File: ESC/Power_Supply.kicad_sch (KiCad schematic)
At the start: 12 parts, among them IC6 BD433M5FP-CE2

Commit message: Power Supply Update
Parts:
- removed L1: 10uH 2.2A 20%, BassingaLib_Inductors:BWVS00505040100M00, symbol BassingaLib_Inductors:BWVS00505040100M00
- added C40, C43: GXC1V221MCQ1GS, BassingaLib_Capacitors:CAPAE1030X1080N, symbol BassingaLib_Capacitors:GXC1V221MCQ1GS
- added C44: 10uF 63V, Capacitor_SMD:C_1210_3225Metric, symbol Device:C
- added J5: XT30PW-M, BassinaLib_Connectors:AMASS_XT30PW-M, symbol BassinaLib_Connectors:XT30PW-M
- added L2: 10uH 2.2A 20%, BassingaLib_Inductors:BWVS00505040100M00, symbol BassingaLib_Inductors:BWVS00505040100M00
- added R50: 0R 1%, Resistor_SMD:R_0603_1608Metric, symbol Device:R
- renumbered C40 to C38, C42 to C39, C36 to C41, C41 to C42, C37 to C45, C38 to C46, C39 to C47
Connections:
- net +12V: now also L2.2
- net GND: now also R50.1
- net at C41.1, PS1.5 (SW): now also L2.1
- new net: C40.1 (+), C43.1 (+), C44.2, J5.P
- new net Power_GND: C40.2 (-), C43.2 (-), C44.1, J5.N, R50.2
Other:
- moved on the sheet: C38, C39, C41, C42, C45, C46, C47, IC6, PS1, R48, R49

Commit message: Update 20.07.2025
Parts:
- added D11: SS0540_R1_00001, BassingaLib_Diodes:SOD3816X135N, symbol BassingaLib_Diodes:SS0540_R1_00001
- added LED2: RED LED, BassinaLib_LEDs:LEDM168X80N, symbol BassinaLib_LEDs:APHD1608LSURCK
- added LED3, LED4: GREEN, BassinaLib_LEDs:LEDM168X80N, symbol BassinaLib_LEDs:APHD1608LZGCK
- added R50: 18k 1%, Resistor_SMD:R_0603_1608Metric, symbol Device:R
- added R52: 10k 1%, Resistor_SMD:R_0603_1608Metric, symbol Device:R
- added R53: 680R 1%, Resistor_SMD:R_0603_1608Metric, symbol Device:R
- R49: Manufacturer_Part_Number AC0603FR-0718KL -> AC0603FR-1318KL
- renumbered C38 to C39, C39 to C40, C40 to C41, C41 to C42, C42 to C43, C43 to C44, C44 to C45, C45 to C46, C46 to C47, C47 to C48, L2 to L1, R50 to R51
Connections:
- net +12V: now also R52.1
- net +3.3V: now also R53.1
- net GND: now also LED3.1 (K), LED4.1 (K)
- net Power_GND: now also D11.2 (A), LED2.1 (K)
- net at C41.1 (+), C44.1 (+), C45.2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: now also D11.1 (K)
- new net: LED3.2 (A), R52.2
- new net: LED4.2 (A), R53.2
- new net: LED2.2 (A), R50.1
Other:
- moved on the sheet: C39, C40, C41, C42, C43, C44, C45, C46, C47, C48, IC6, J5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

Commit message: End of Schematic
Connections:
- net at R50.1: no longer LED2.2 (A)
- net at R50.2: now also LED2.2 (A)
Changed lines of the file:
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@@
 	(wire
 		(pts
+			(xy 223.52 95.25) (xy 223.52 101.6)
+		)
+		(stroke
+			(width 0)
+			(type default)
+		)
+	)
+	(wire
+		(pts
 			(xy 153.67 109.22) (xy 137.16 109.22)
 		)
@@
 	(wire
 		(pts
-			(xy 223.52 95.25) (xy 223.52 101.6)
-		)
-		(stroke
-			(width 0)
-			(type default)
-		)
-	)
-	(wire
-		(pts
 			(xy 46.99 99.06) (xy 52.07 99.06)
 		)
@@
 			)
 		)
-		(property "Value" "6S_Power"
+		(property "Value" "+22V"
 			(at 34.29 85.09 0)
 			(effects
@@
 		(lib_id "Device:R")
 		(at 223.52 91.44 0)
-		(mirror x)
+		(mirror y)
 		(unit 1)
 		(exclude_from_sim no)
@@
 		(dnp no)
 		(property "Reference" "R50"
-			(at 220.472 89.662 90)
+			(at 226.568 93.218 90)
 			(effects
 				(font
@@
 		)
 		(property "Value" "18k 1%"
-			(at 226.822 88.138 90)
+			(at 220.218 94.742 90)
 			(effects
 				(font
@@
 		)
 		(property "Footprint" "Resistor_SMD:R_0603_1608Metric"
-			(at 221.742 91.44 90)
+			(at 225.298 91.44 90)
 			(effects
 				(font
@@
 		(dnp no)
 		(fields_autoplaced yes)
-		(property "Reference" "#PWR0100"
+		(property "Reference" "#PWR093"
 			(at 223.52 127.508 0)
 			(effects
@@
 			(project "ESC"
 				(path "/7036a814-0f41-4c6c-a077-a78d90a22423/50e6b873-fcc8-4519-931d-a1e0dcbcbe76"
-					(reference "#PWR0100")
+					(reference "#PWR093")
 					(unit 1)
 				)
@@
 			)
 		)
-		(property "Value" "6S_Power"
+		(property "Value" "+22V"
 			(at 127 21.59 0)
 			(effects
@@
 			)
 		)
-		(property "Value" "6S_Power"
+		(property "Value" "+22V"
 			(at 223.52 76.2 0)
 			(effects

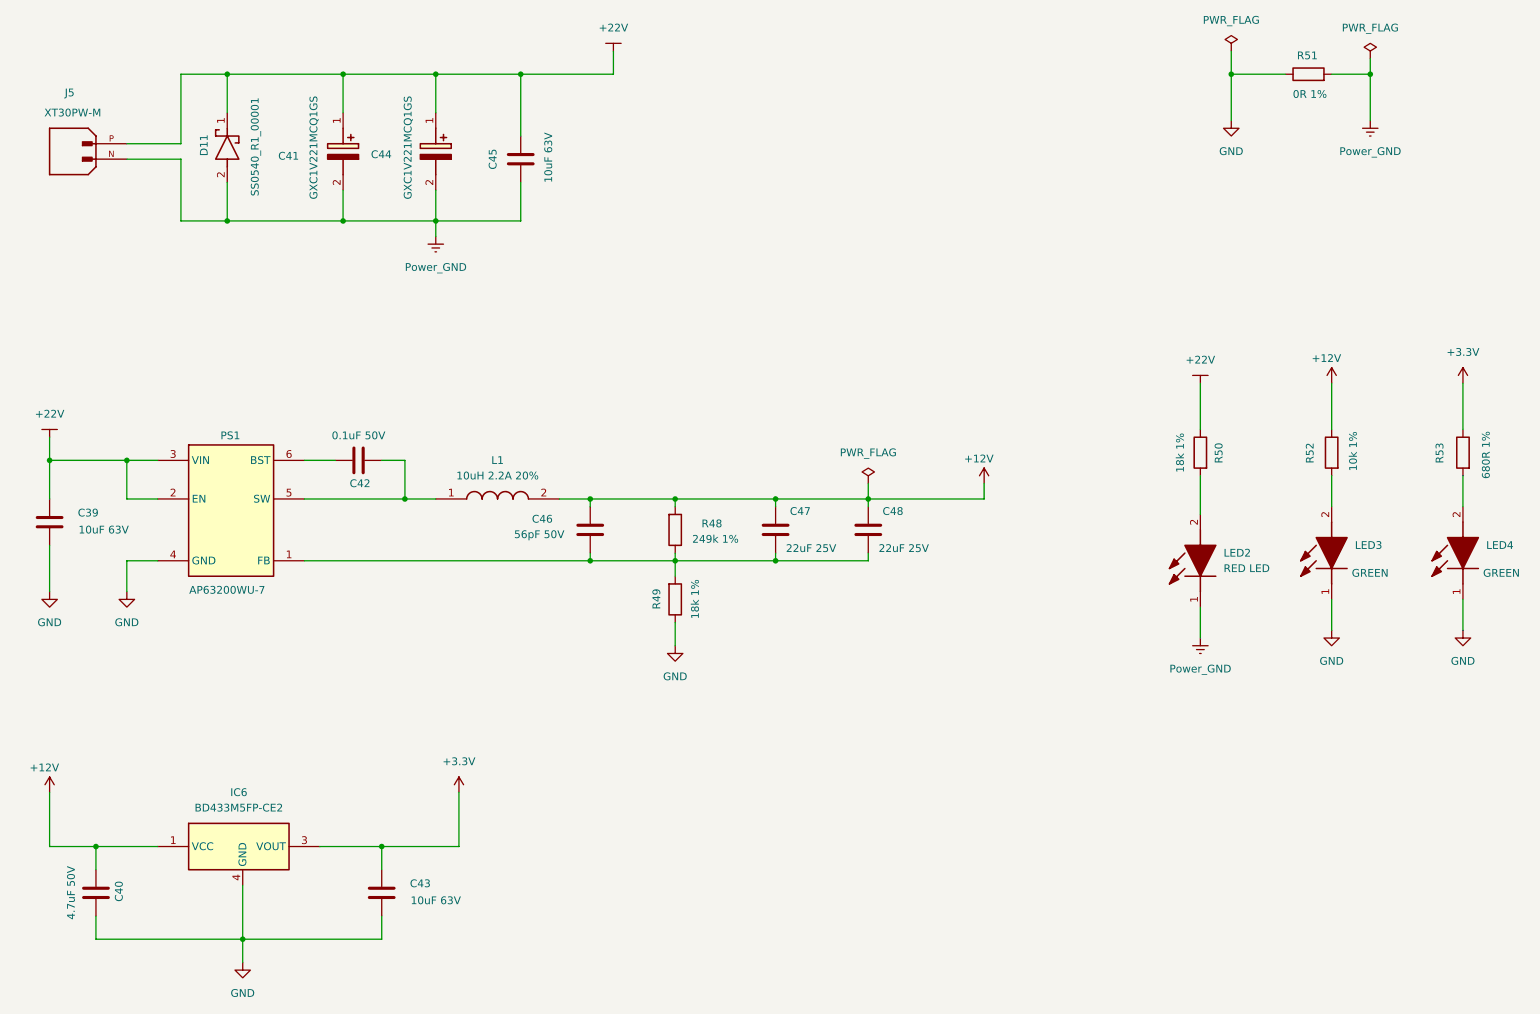
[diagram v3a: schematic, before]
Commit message: Start of PCB Layout
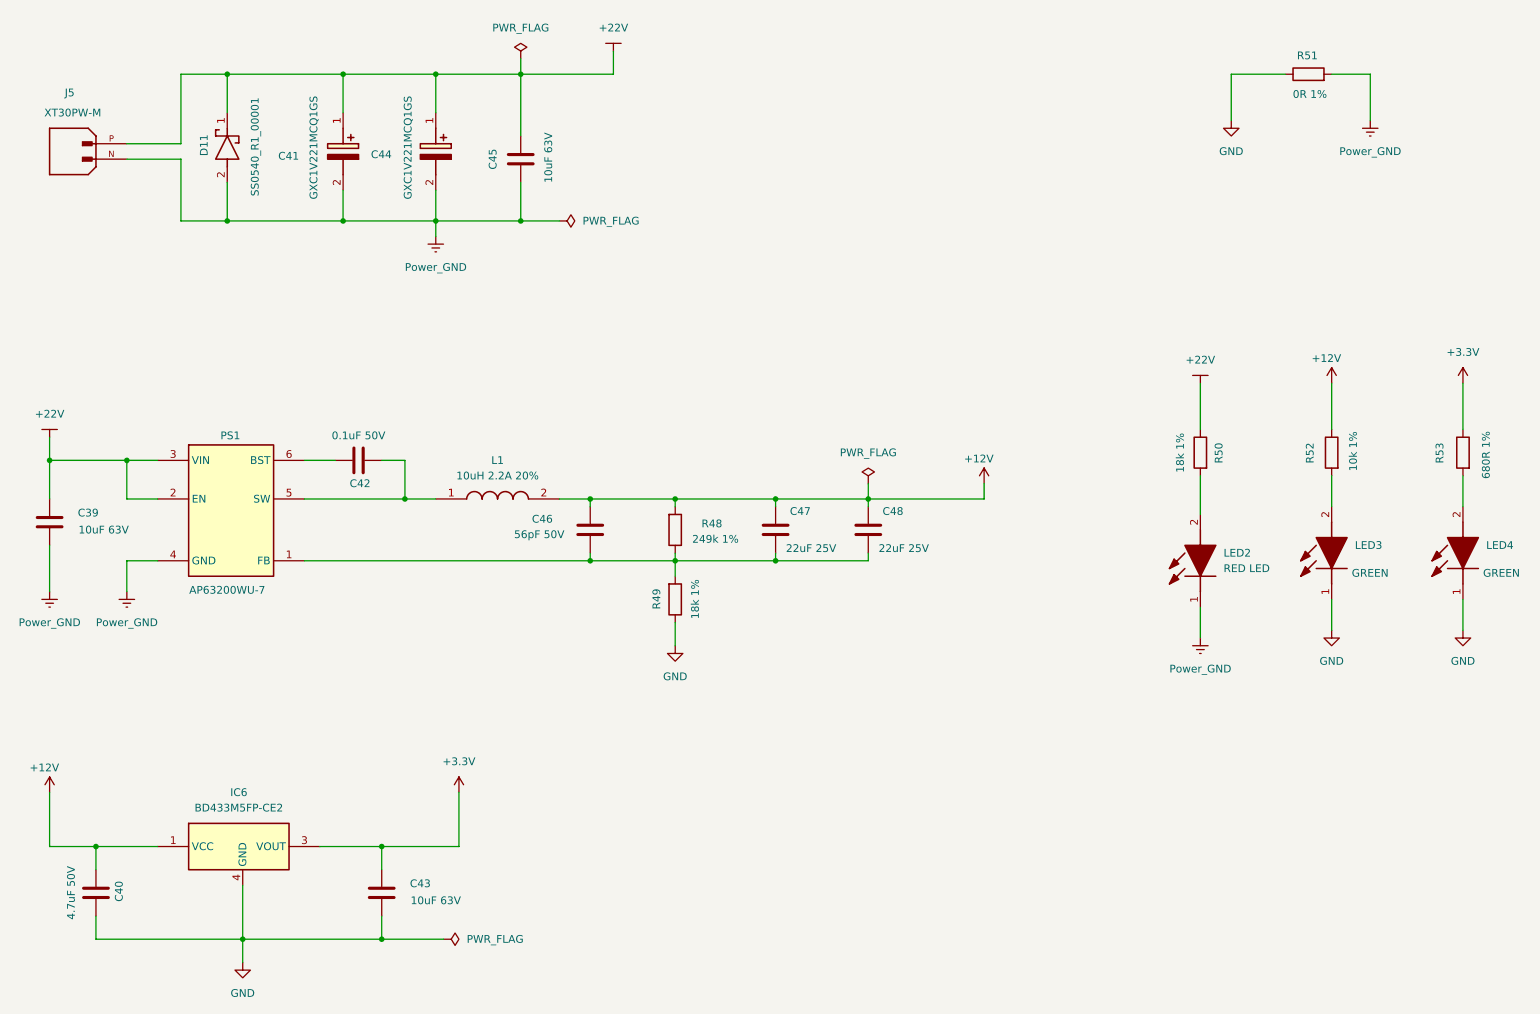
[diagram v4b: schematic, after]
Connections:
- net GND: no longer C39.1, PS1.4 (GND)
- net Power_GND: now also C39.1, PS1.4 (GND)
- net +22V: now reaches C41.1 (+), C44.1 (+), C45.2, D11.1 (K), J5.P
- net +22V: now also C39.2, PS1.2 (EN), PS1.3 (VIN), R50.1

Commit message: PCB Layout Update
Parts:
- removed R51: 0R 1%, Resistor_SMD:R_0603_1608Metric, symbol Device:R
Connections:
- net Power_GND is gone; now on net GND: C39.1, C41.2 (-), C44.2 (-), C45.1, D11.2 (A), J5.N, LED2.1 (K), PS1.4 (GND)
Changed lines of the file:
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@@
 	(wire
 		(pts
-			(xy 237.49 29.21) (xy 228.6 29.21)
+			(xy 228.6 29.21) (xy 251.46 29.21)
 		)
 		(stroke
@@
 	(wire
 		(pts
-			(xy 245.11 29.21) (xy 251.46 29.21)
-		)
-		(stroke
-			(width 0)
-			(type default)
-		)
-	)
-	(wire
-		(pts
 			(xy 78.74 156.21) (xy 88.9 156.21)
 		)
@@
 					(unit 1)
 				)
-			)
-		)
-	)
-	(symbol
-		(lib_id "Device:R")
-		(at 241.3 29.21 90)
-		(unit 1)
-		(exclude_from_sim no)
-		(in_bom yes)
-		(on_board yes)
-		(dnp no)
-		(property "Reference" "R51"
-			(at 242.824 26.162 90)
-			(effects
-				(font
-					(size 1.27 1.27)
-				)
-				(justify left)
-			)
-		)
-		(property "Value" "0R 1%"
-			(at 244.348 32.512 90)
-			(effects
-				(font
-					(size 1.27 1.27)
-				)
-				(justify left)
-			)
-		)
-		(property "Footprint" "Resistor_SMD:R_0603_1608Metric"
-			(at 241.3 30.988 90)
-			(effects
-				(font
-					(size 1.27 1.27)
-				)
-				(hide yes)
-			)
-		)
-		(property "Datasheet" "https://www.mouser.fr/datasheet/2/447/Yageo_06282023_ACseries-3224032.pdf"
-			(at 241.3 29.21 0)
-			(effects
-				(font
-					(size 1.27 1.27)
-				)
-				(hide yes)
-			)
-		)
-		(property "Description" "Thick Film Resistors - SMD 0 Ohms 100mW 0603 1% AEC-Q200 Standard Power Version"
-			(at 241.3 29.21 0)
-			(effects
-				(font
-					(size 1.27 1.27)
-				)
-				(hide yes)
-			)
-		)
-		(property "Manufacturer_Name" "YAGEO"
-			(at 241.3 29.21 0)
-			(effects
-				(font
-					(size 1.27 1.27)
-				)
-				(hide yes)
-			)
-		)
-		(property "Manufacturer_Part_Number" "AC0603FR-070RL"
-			(at 241.3 29.21 0)
-			(effects
-				(font
-					(size 1.27 1.27)
-				)
-				(hide yes)
-			)
-		)
-		(property "Packaging" "0603 (608mm)"
-			(at 241.3 29.21 0)
-			(effects
-				(font
-					(size 1.27 1.27)
-				)
-				(hide yes)
-			)
-		)
-		(pin "1"
-		)
-		(pin "2"
-		)
-		(instances
-			(project "ESC"
-				(path "/7036a814-0f41-4c6c-a077-a78d90a22423/50e6b873-fcc8-4519-931d-a1e0dcbcbe76"
-					(reference "R51")
-					(unit 1)
-				)

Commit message: Update 25.07.2025
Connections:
- net GND: now also C47.1, C48.1
- net at C46.1, PS1.1 (FB), R48.1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: no longer C47.1, C48.1
- net SW: now reaches C42.1, L1.1, PS1.5 (SW)
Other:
- moved on the sheet: C47, C48, R49
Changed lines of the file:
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@@
 	)
 	(junction
+		(at 137.16 120.65)
+		(diameter 0)
+		(color 0 0 0 0)
+	)
+	(junction
+		(at 123.19 109.22)
+		(diameter 0)
+		(color 0 0 0 0)
+	)
+	(junction
 		(at 137.16 99.06)
 		(diameter 0)
@@
 	)
 	(junction
-		(at 111.76 29.21)
+		(at 153.67 120.65)
 		(diameter 0)
 		(color 0 0 0 0)
 	)
 	(junction
-		(at 97.79 29.21)
+		(at 111.76 29.21)
 		(diameter 0)
 		(color 0 0 0 0)
 	)
 	(junction
-		(at 34.29 92.71)
+		(at 97.79 29.21)
 		(diameter 0)
 		(color 0 0 0 0)
 	)
 	(junction
-		(at 153.67 109.22)
+		(at 34.29 92.71)
 		(diameter 0)
 		(color 0 0 0 0)
@@
 	)
 	(junction
-		(at 88.9 171.45)
-		(diameter 0)
-		(color 0 0 0 0)
-	)
-	(junction
-		(at 41.91 156.21)
+		(at 137.16 109.22)
 		(diameter 0)
 		(color 0 0 0 0)
 	)
 	(junction
-		(at 111.76 53.34)
+		(at 88.9 171.45)
 		(diameter 0)
 		(color 0 0 0 0)
 	)
 	(junction
-		(at 46.99 92.71)
+		(at 41.91 156.21)
 		(diameter 0)
 		(color 0 0 0 0)
 	)
 	(junction
-		(at 137.16 109.22)
+		(at 111.76 53.34)
 		(diameter 0)
 		(color 0 0 0 0)
 	)
 	(junction
-		(at 123.19 109.22)
+		(at 46.99 92.71)
 		(diameter 0)
 		(color 0 0 0 0)
@@
 	(wire
 		(pts
-			(xy 82.55 53.34) (xy 97.79 53.34)
+			(xy 123.19 107.95) (xy 123.19 109.22)
 		)
 		(stroke
@@
 	(wire
 		(pts
-			(xy 92.71 99.06) (xy 97.79 99.06)
+			(xy 82.55 53.34) (xy 97.79 53.34)
 		)
 		(stroke
@@
 	(wire
 		(pts
-			(xy 228.6 29.21) (xy 251.46 29.21)
+			(xy 92.71 99.06) (xy 97.79 99.06)
 		)
 		(stroke
@@
 	(wire
 		(pts
-			(xy 46.99 92.71) (xy 46.99 99.06)
+			(xy 228.6 29.21) (xy 251.46 29.21)
 		)
 		(stroke
@@
 	(wire
 		(pts
-			(xy 251.46 29.21) (xy 251.46 36.83)
+			(xy 46.99 92.71) (xy 46.99 99.06)
 		)
 		(stroke
@@
 	(wire
 		(pts
-			(xy 46.99 43.18) (xy 55.88 43.18)
+			(xy 251.46 29.21) (xy 251.46 36.83)
 		)
 		(stroke
@@
 	(wire
 		(pts
-			(xy 123.19 109.22) (xy 137.16 109.22)
+			(xy 46.99 43.18) (xy 55.88 43.18)
 		)
 		(stroke
@@
 	(wire
 		(pts
-			(xy 137.16 123.19) (xy 137.16 119.38)
+			(xy 137.16 123.19) (xy 137.16 120.65)
 		)
 		(stroke
@@
 	(wire
 		(pts
-			(xy 153.67 107.95) (xy 153.67 109.22)
+			(xy 76.2 109.22) (xy 123.19 109.22)
 		)
 		(stroke
@@
 	(wire
 		(pts
-			(xy 168.91 100.33) (xy 168.91 99.06)
+			(xy 168.91 105.41) (xy 168.91 99.06)
 		)
 		(stroke
@@
 	(wire
 		(pts
-			(xy 137.16 109.22) (xy 137.16 107.95)
+			(xy 137.16 107.95) (xy 137.16 109.22)
 		)
 		(stroke
@@
 	(wire
 		(pts
-			(xy 153.67 109.22) (xy 168.91 109.22)
+			(xy 153.67 120.65) (xy 168.91 120.65)
 		)
 		(stroke
@@
 	(wire
 		(pts
-			(xy 153.67 100.33) (xy 153.67 99.06)
+			(xy 153.67 105.41) (xy 153.67 99.06)
+		)
+		(stroke
+			(width 0)
+			(type default)
+		)
+	)
+	(wire
+		(pts
+			(xy 137.16 109.22) (xy 137.16 110.49)
 		)
 		(stroke
@@
 	(wire
 		(pts
-			(xy 153.67 109.22) (xy 137.16 109.22)
+			(xy 123.19 109.22) (xy 137.16 109.22)
 		)
 		(stroke
@@
 	(wire
 		(pts
-			(xy 76.2 109.22) (xy 123.19 109.22)
+			(xy 153.67 113.03) (xy 153.67 120.65)
 		)
 		(stroke
@@
 	(wire
 		(pts
+			(xy 137.16 118.11) (xy 137.16 120.65)
+		)
+		(stroke
+			(width 0)
+			(type default)
+		)
+	)
+	(wire
+		(pts
 			(xy 46.99 99.06) (xy 52.07 99.06)
 		)
@@
 	(wire
 		(pts
-			(xy 123.19 109.22) (xy 123.19 107.95)
+			(xy 137.16 120.65) (xy 153.67 120.65)
 		)
 		(stroke
@@
 	(wire
 		(pts
-			(xy 137.16 111.76) (xy 137.16 109.22)
-		)
-		(stroke
-			(width 0)
-			(type default)
-		)
-	)
-	(wire
-		(pts
 			(xy 41.91 156.21) (xy 52.07 156.21)
 		)
@@
 	(wire
 		(pts
-			(xy 168.91 107.95) (xy 168.91 109.22)
+			(xy 168.91 113.03) (xy 168.91 120.65)
 		)
 		(stroke
@@
 		)
 	)
+	(label "SW"
+		(at 78.74 99.06 0)
+		(effects
+			(font
+				(size 1.27 1.27)
+			)
+			(justify left bottom)
+		)
+	)
 	(symbol
 		(lib_id "power:GND")
@@
 	(symbol
 		(lib_id "Device:R")
-		(at 137.16 115.57 0)
+		(at 137.16 114.3 0)
 		(mirror x)
 		(unit 1)
@@
 		(dnp no)
 		(property "Reference" "R49"
-			(at 134.112 113.792 90)
+			(at 134.112 112.522 90)
 			(effects
 				(font
@@
 		)
 		(property "Value" "18k 1%"
-			(at 140.462 112.268 90)
+			(at 140.462 110.998 90)
 			(effects
 				(font
@@
 		)
 		(property "Footprint" "Resistor_SMD:R_0603_1608Metric"
-			(at 135.382 115.57 90)
+			(at 135.382 114.3 90)
 			(effects
 				(font
@@
 		)
 		(property "Datasheet" "https://www.mouser.fr/datasheet/2/447/PYu_AC_51_RoHS_L_11-3418659.pdf"
-			(at 137.16 115.57 0)
+			(at 137.16 114.3 0)
 			(effects
 				(font
@@
 		)
 		(property "Description" "Thick Film Resistors - SMD 18 kOhms 100mW 0603 1% AEC-Q200"
-			(at 137.16 115.57 0)
+			(at 137.16 114.3 0)
 			(effects
 				(font
@@
 		)
 		(property "Manufacturer_Name" "YAGEO"
-			(at 137.16 115.57 0)
+			(at 137.16 114.3 0)
 			(effects
 				(font
@@
 		)
 		(property "Manufacturer_Part_Number" "AC0603FR-1318KL"
-			(at 137.16 115.57 0)
+			(at 137.16 114.3 0)
 			(effects
 				(font
@@
 		)
 		(property "Packaging" "0603 (608mm)"
-			(at 137.16 115.57 0)
+			(at 137.16 114.3 0)
 			(effects
 				(font
@@
 	(symbol
 		(lib_id "Device:C")
-		(at 168.91 104.14 180)
+		(at 168.91 109.22 180)
 		(unit 1)
 		(exclude_from_sim no)
@@
 		(dnp no)
 		(property "Reference" "C48"
-			(at 172.974 101.092 0)
+			(at 172.974 106.172 0)
 			(effects
 				(font
@@
 		)
 		(property "Value" "22uF 25V"
-			(at 174.752 107.188 0)
+			(at 174.752 112.268 0)
 			(effects
 				(font
@@
 		)
 		(property "Footprint" "Capacitor_SMD:C_1210_3225Metric"
-			(at 167.9448 100.33 0)
+			(at 167.9448 105.41 0)
 			(effects
 				(font
@@
 		)
 		(property "Datasheet" "https://www.mouser.fr/datasheet/2/585/MLCC-1837944.pdf"
-			(at 168.91 104.14 0)
+			(at 168.91 109.22 0)
 			(effects
 				(font
@@
 		)
 		(property "Description" "Multilayer Ceramic Capacitors MLCC - SMD/SMT 22uF+/-10% 25V X7R 3 1210"
-			(at 168.91 104.14 0)
+			(at 168.91 109.22 0)
 			(effects
 				(font
@@
 		)
 		(property "Manufacturer_Name" "Samsung Electro-Mechanics"
-			(at 168.91 104.14 0)
+			(at 168.91 109.22 0)
 			(effects
 				(font
@@
 		)
 		(property "Manufacturer_Part_Number" "CL32B226KAJNNNE"
-			(at 168.91 104.14 0)
+			(at 168.91 109.22 0)
 			(effects
 				(font
@@
 		)
 		(property "Packaging" "1210 (3225mm)"
-			(at 168.91 104.14 0)
+			(at 168.91 109.22 0)
 			(effects
 				(font
@@
 	(symbol
 		(lib_id "Device:C")
-		(at 153.67 104.14 180)
+		(at 153.67 109.22 180)
 		(unit 1)
 		(exclude_from_sim no)
@@
 		(dnp no)
 		(property "Reference" "C47"
-			(at 157.734 101.092 0)
+			(at 157.734 106.172 0)
 			(effects
 				(font
@@
 		)
 		(property "Value" "22uF 25V"
-			(at 159.512 107.188 0)
+			(at 159.512 112.268 0)
 			(effects
 				(font
@@
 		)
 		(property "Footprint" "Capacitor_SMD:C_1210_3225Metric"
-			(at 152.7048 100.33 0)
+			(at 152.7048 105.41 0)
 			(effects
 				(font
@@
 		)
 		(property "Datasheet" "https://www.mouser.fr/datasheet/2/585/MLCC-1837944.pdf"
-			(at 153.67 104.14 0)
+			(at 153.67 109.22 0)
 			(effects
 				(font
@@
 		)
 		(property "Description" "Multilayer Ceramic Capacitors MLCC - SMD/SMT 22uF+/-10% 25V X7R 3 1210"
-			(at 153.67 104.14 0)
+			(at 153.67 109.22 0)
 			(effects
 				(font
@@
 		)
 		(property "Manufacturer_Name" "Samsung Electro-Mechanics"
-			(at 153.67 104.14 0)
+			(at 153.67 109.22 0)
 			(effects
 				(font
@@
 		)
 		(property "Manufacturer_Part_Number" "CL32B226KAJNNNE"
-			(at 153.67 104.14 0)
+			(at 153.67 109.22 0)
 			(effects
 				(font
@@
 		)
 		(property "Packaging" "1210 (3225mm)"
-			(at 153.67 104.14 0)
+			(at 153.67 109.22 0)
 			(effects
 				(font

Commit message: PCB nearly completed
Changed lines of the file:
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@@
-	)
-	(junction
-		(at 111.76 53.34)
-		(diameter 0)
-		(color 0 0 0 0)
 	)
 	(junction
@@
 		(pts
 			(xy 168.91 105.41) (xy 168.91 99.06)
-		)
-		(stroke
-			(width 0)
-			(type default)
-		)
-	)
-	(wire
-		(pts
-			(xy 111.76 53.34) (xy 118.11 53.34)
 		)
 		(stroke
@@
 					(unit 1)
 				)
-			)
-		)
-	)
-	(symbol
-		(lib_id "power:PWR_FLAG")
-		(at 118.11 53.34 270)
-		(unit 1)
-		(exclude_from_sim no)
-		(in_bom yes)
-		(on_board yes)
-		(dnp no)
-		(fields_autoplaced yes)
-		(property "Reference" "#FLG02"
-			(at 120.015 53.34 0)
-			(effects
-				(font
-					(size 1.27 1.27)
-				)
-				(hide yes)
-			)
-		)
-		(property "Value" "PWR_FLAG"
-			(at 121.92 53.3399 90)
-			(effects
-				(font
-					(size 1.27 1.27)
-				)
-				(justify left)
-			)
-		)
-		(property "Footprint" ""
-			(at 118.11 53.34 0)
-			(effects
-				(font
-					(size 1.27 1.27)
-				)
-				(hide yes)
-			)
-		)
-		(property "Datasheet" "~"
-			(at 118.11 53.34 0)
-			(effects
-				(font
-					(size 1.27 1.27)
-				)
-				(hide yes)
-			)
-		)
-		(property "Description" "Special symbol for telling ERC where power comes from"
-			(at 118.11 53.34 0)
-			(effects
-				(font
-					(size 1.27 1.27)
-				)
-				(hide yes)
-			)
-		)
-		(pin "1"
-		)
-		(instances
-			(project ""
-				(path "/7036a814-0f41-4c6c-a077-a78d90a22423/50e6b873-fcc8-4519-931d-a1e0dcbcbe76"
-					(reference "#FLG02")
-					(unit 1)
-				)

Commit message: BOM
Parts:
- J5: now left out of the parts list
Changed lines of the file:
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@@
 		(unit 1)
 		(exclude_from_sim no)
-		(in_bom yes)
+		(in_bom no)
 		(on_board yes)
 		(dnp no)
